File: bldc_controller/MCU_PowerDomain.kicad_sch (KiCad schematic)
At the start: 10 parts, among them U5 STM32G474CEUx

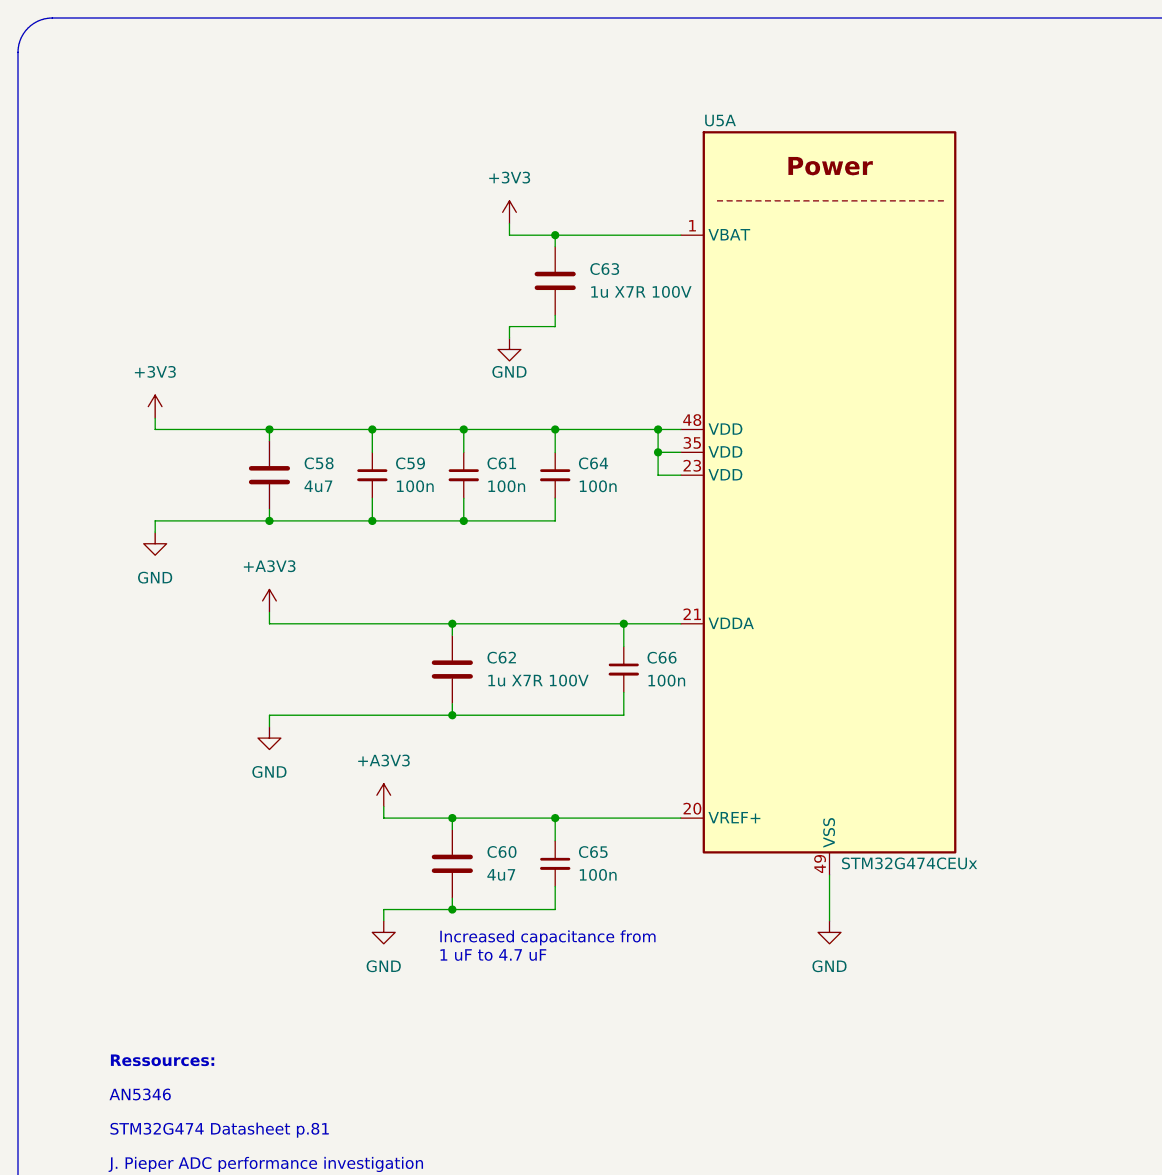
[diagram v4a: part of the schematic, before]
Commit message: added power domains. Risk of ground shift near CAN
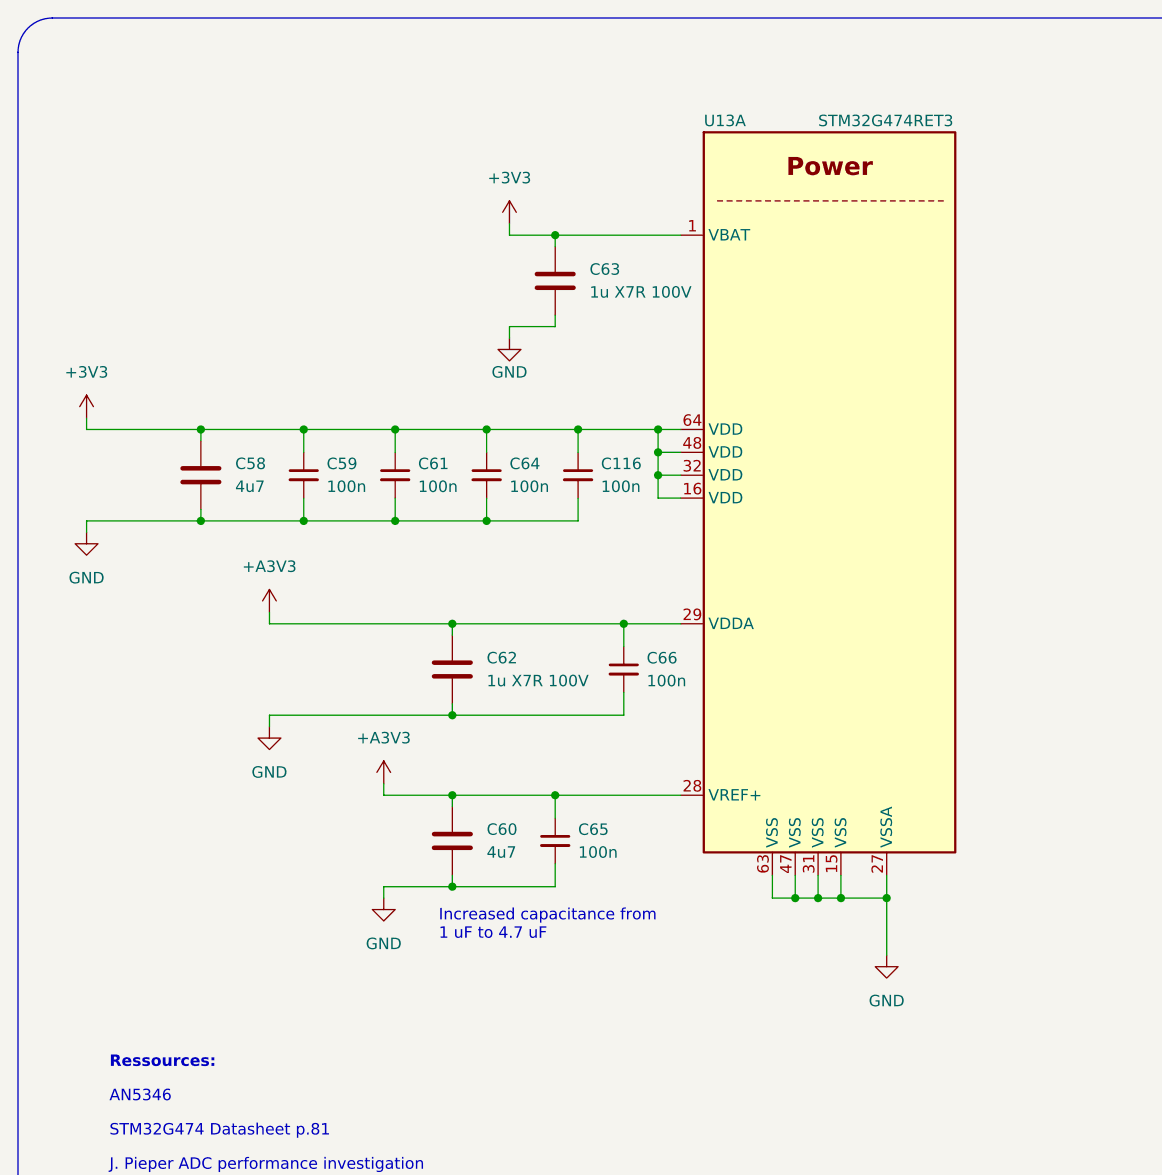
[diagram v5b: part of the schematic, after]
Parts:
- removed U5: STM32G474CEUx, Package_DFN_QFN:QFN-48-1EP_7x7mm_P0.5mm_EP5.6x5.6mm, symbol 0_mcu:STM32G474CEUx
- added C116: 100n, 0_capacitor_smd:C_0402_1005_DensityHigh, symbol Device:C_Small
- added U13: STM32G474RET3, Package_QFP:LQFP-64_10x10mm_P0.5mm, symbol 0_mcu:STM32G474RETx
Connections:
- net +3V3: now also C116.1, U13.1 (VBAT), U13.16 (VDD), U13.32 (VDD), U13.48 (VDD), U13.64 (VDD)
- net +A3V3: now also U13.28 (VREF+), U13.29 (VDDA)
- net GND: now also C116.2, U13.15 (VSS), U13.27 (VSSA), U13.31 (VSS), U13.47 (VSS), U13.63 (VSS)
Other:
- moved on the sheet: C58, C59, C60, C61, C64, C65

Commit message: might have fixed net issue, added dxf and svgs
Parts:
- renumbered U13 to U5
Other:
- note removed: "Ressources:"
- moved on the sheet: C116, C58, C59, C60, C61, C62, C63, C64, C65, C66, U5A

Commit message: starting rerouting for PCBWay 8/8 mils, 0.25mm drill
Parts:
- U5: footprint Package_QFP:LQFP-64_10x10mm_P0.5mm -> 0_package_QFP:LQFP-64_10x10mm_P0.5mm
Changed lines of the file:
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@@
       (effects (font (size 1.27 1.27)) (justify left))
     )
-    (property "Footprint" "Package_QFP:LQFP-64_10x10mm_P0.5mm" (at 186.69 166.37 0)
+    (property "Footprint" "0_package_QFP:LQFP-64_10x10mm_P0.5mm" (at 186.69 166.37 0)
       (effects (font (size 1.27 1.27)) (justify right) hide)
     )
